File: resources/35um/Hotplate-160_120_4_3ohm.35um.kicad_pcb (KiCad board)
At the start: 2 copper layers, 160 x 120 mm, 7 parts, among them J1 Hotplate_Power_Connection, J2 Hotplate_Power_Connection

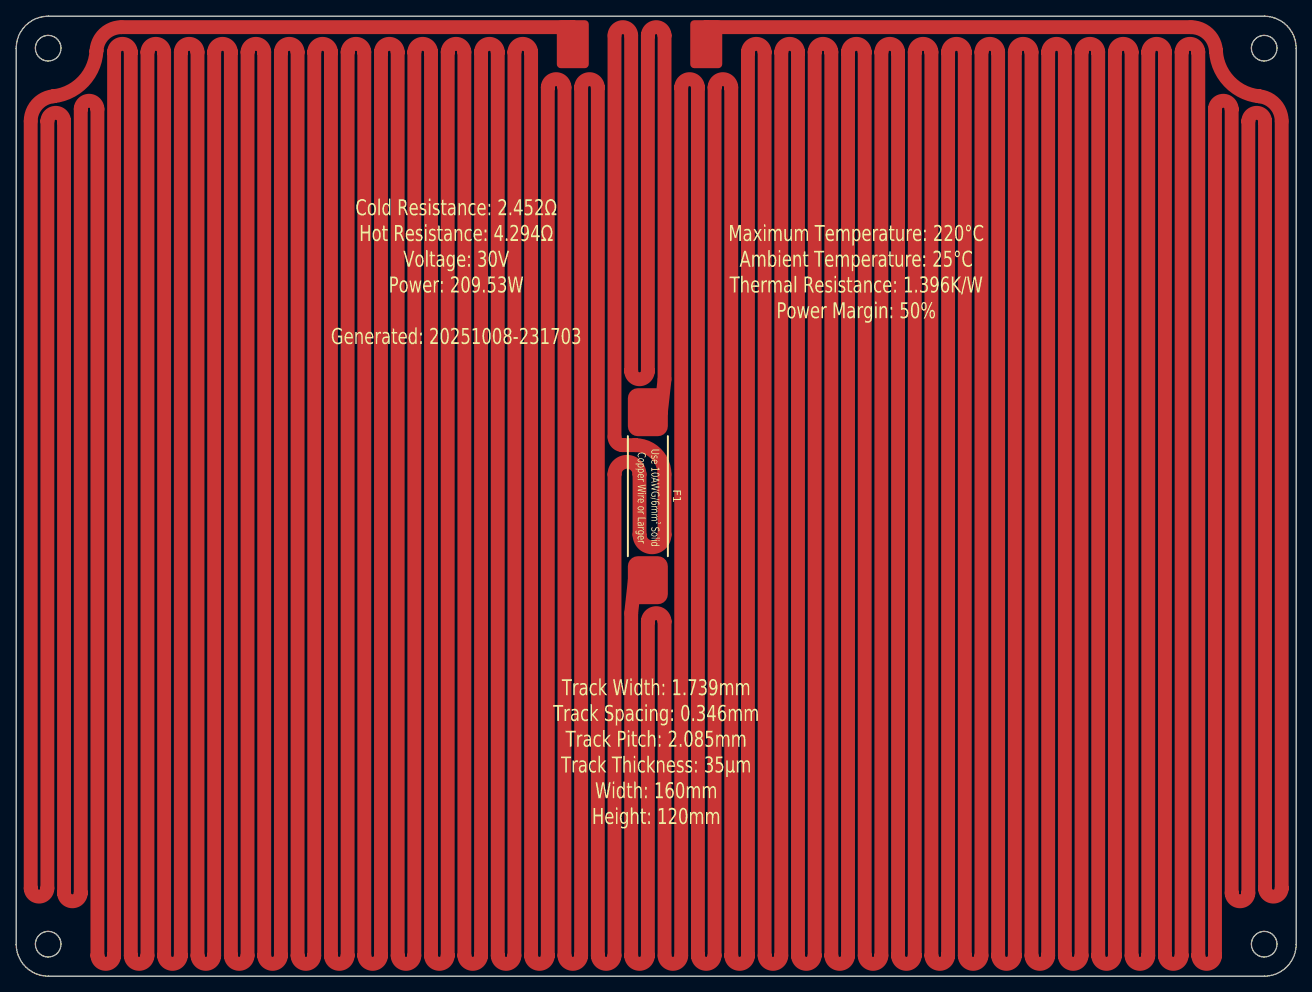
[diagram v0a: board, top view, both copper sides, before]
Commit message: Replaced obsolete 25mm thermal fuse footprint with new 35mm thermal fuse footprint.
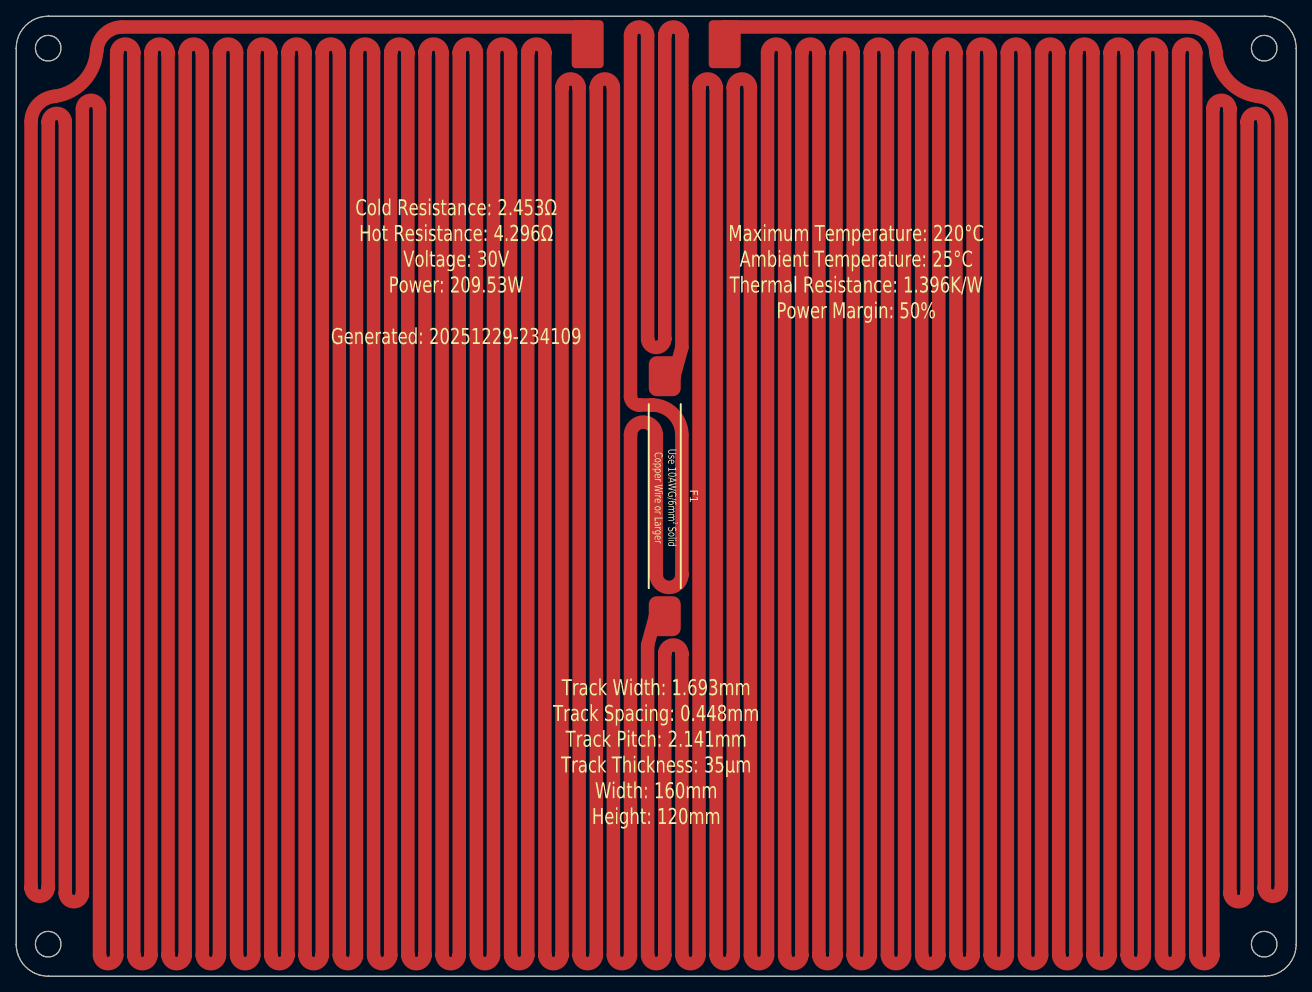
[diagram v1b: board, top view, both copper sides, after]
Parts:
- F1: footprint blg:Thermal Fuse, Front, 25mm -> blg:Thermal Fuse, SN100C, Front, 35mm
- moved J2 2.31 mm to (113.6, 48.5)
- moved F1 2.11 mm to (106.1, 105.0)
- moved J1 1.86 mm to (96.4, 48.5)
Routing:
- net Net-(J2-Pin_1): track 4415.0 -> 4167.2 mm
- net Net-(J1-Pin_1): track 4325.6 -> 4334.0 mm
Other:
- board text added: "Cold Resistance: 2.453Ω Hot Resistance: 4.296Ω Voltage: 30V Power: 209.53W Generated: 20251229-234109"
- board text added: "Track Width: 1.693mm Track Spacing: 0.448mm Track Pitch: 2.141mm Track Thickness: 35µm Width: 160mm Height: 120mm"
- board text removed: "Cold Resistance: 2.452Ω Hot Resistance: 4.294Ω Voltage: 30V Power: 209.53W Generated: 20251008-231703"
- board text removed: "Track Width: 1.739mm Track Spacing: 0.346mm Track Pitch: 2.085mm Track Thickness: 35µm Width: 160mm Height: 120mm"
